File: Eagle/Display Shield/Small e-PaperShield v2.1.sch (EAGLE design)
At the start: 111 parts, among them J2 3300060P1-ST-TF-003A, J3 2.54-8p-male-SMD, J4 2.54-8p-male-SMD, J5 2.54-6p-male-SMD, J6 2.54-6p-male-SMD, J7 2.54-2x3p-female-SMD, Q10 MOSFET-P-044021001, Q11 2N7002, Q2 2N7002, Q3 MOSFET-P-044021001, Q5 MOSFET-P-044021001, Q7 MOSFET-P-044021001, Q8 2N7002, Q9 2N7002, U2 XC6206-3.3-1300260P1, U3 74VHC125PW, U4 74VHC125PW, U5 GT20L16P1Y, U9 S-8120CNB-DRB-TF-G//200021001, X1 FH12-40S-0.5SH

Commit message: added pull-ups for buttons on display shield
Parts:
- added R15, R17, R5, R6: 10k, Discrete:R-0603
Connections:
- net BTN0: now also R5.2
- net BTN1: now also R6.2
- net BTN2: now also R15.2
- net BTN3: now also R17.2
- net LED0: now also J3.1; no longer J3.2
- net LED1: now also J3.2; no longer J3.1
- net M_VCC_3V3: now also R15.1, R17.1, R5.1, R6.1
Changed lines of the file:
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@@
 <part name="SUPPLY3" library="supply2" deviceset="GND" device=""/>
 <part name="SUPPLY4" library="supply2" deviceset="GND" device=""/>
+<part name="R5" library="Discrete" deviceset="R*" device="-0603" value="10k"/>
+<part name="R6" library="Discrete" deviceset="R*" device="-0603" value="10k"/>
+<part name="R15" library="Discrete" deviceset="R*" device="-0603" value="10k"/>
+<part name="R17" library="Discrete" deviceset="R*" device="-0603" value="10k"/>
 </parts>
 <sheets>
@@
 <instance part="SUPPLY3" gate="GND" x="284.48" y="116.84"/>
 <instance part="SUPPLY4" gate="GND" x="287.02" y="142.24"/>
+<instance part="R5" gate="R" x="295.91" y="157.48" rot="MR0"/>
+<instance part="R6" gate="R" x="295.91" y="132.08" rot="MR0"/>
+<instance part="R15" gate="R" x="297.18" y="106.68" rot="MR0"/>
+<instance part="R17" gate="R" x="295.91" y="81.28" rot="MR0"/>
 </instances>
 <busses>
@@
 <label x="-245.11" y="127" size="1.27" layer="95" ratio="10" rot="R180"/>
 </segment>
+<segment>
+<pinref part="R5" gate="R" pin="1"/>
+<wire x1="299.72" y1="157.48" x2="309.88" y2="157.48" width="0.1524" layer="91"/>
+<label x="302.26" y="157.48" size="1.778" layer="95"/>
+</segment>
+<segment>
+<pinref part="R6" gate="R" pin="1"/>
+<wire x1="299.72" y1="132.08" x2="308.61" y2="132.08" width="0.1524" layer="91"/>
+<label x="302.26" y="132.08" size="1.778" layer="95"/>
+</segment>
+<segment>
+<pinref part="R15" gate="R" pin="1"/>
+<wire x1="300.99" y1="106.68" x2="307.34" y2="106.68" width="0.1524" layer="91"/>
+<wire x1="307.34" y1="106.68" x2="308.61" y2="106.68" width="0.1524" layer="91"/>
+<label x="302.26" y="106.68" size="1.778" layer="95"/>
+</segment>
+<segment>
+<pinref part="R17" gate="R" pin="1"/>
+<wire x1="299.72" y1="81.28" x2="308.61" y2="81.28" width="0.1524" layer="91"/>
+<label x="302.26" y="81.28" size="1.778" layer="95"/>
+</segment>
 </net>
 <net name="M_VCC_5V" class="0">
@@
 </segment>
 <segment>
+<pinref part="J3" gate="J" pin="2"/>
+<wire x1="471.17" y1="137.16" x2="471.17" y2="143.51" width="0.1524" layer="91"/>
+<label x="471.17" y="138.43" size="1.778" layer="95" rot="R90"/>
+</segment>
+</net>
+<net name="LED0" class="0">
+<segment>
+<wire x1="300.99" y1="53.34" x2="300.99" y2="57.15" width="0.1524" layer="91"/>
+<label x="300.99" y="57.15" size="1.778" layer="95" rot="R90" xref="yes"/>
+<pinref part="R1" gate="G$1" pin="2"/>
+</segment>
+<segment>
 <pinref part="J3" gate="J" pin="1"/>
 <wire x1="473.71" y1="137.16" x2="473.71" y2="143.51" width="0.1524" layer="91"/>
 <label x="473.71" y="138.43" size="1.778" layer="95" rot="R90"/>
-</segment>
-</net>
-<net name="LED0" class="0">
-<segment>
-<wire x1="300.99" y1="53.34" x2="300.99" y2="57.15" width="0.1524" layer="91"/>
-<label x="300.99" y="57.15" size="1.778" layer="95" rot="R90" xref="yes"/>
-<pinref part="R1" gate="G$1" pin="2"/>
-</segment>
-<segment>
-<pinref part="J3" gate="J" pin="2"/>
-<wire x1="471.17" y1="137.16" x2="471.17" y2="143.51" width="0.1524" layer="91"/>
-<label x="471.17" y="138.43" size="1.778" layer="95" rot="R90"/>
 </segment>
 </net>
@@
 <junction x="281.94" y="81.28"/>
 <wire x1="281.94" y1="81.28" x2="287.02" y2="81.28" width="0.1524" layer="91"/>
+<pinref part="R17" gate="R" pin="2"/>
+<wire x1="287.02" y1="81.28" x2="292.1" y2="81.28" width="0.1524" layer="91"/>
 </segment>
 <segment>
@@
 <junction x="281.94" y="106.68"/>
 <wire x1="281.94" y1="106.68" x2="287.02" y2="106.68" width="0.1524" layer="91"/>
+<pinref part="R15" gate="R" pin="2"/>
+<wire x1="287.02" y1="106.68" x2="293.37" y2="106.68" width="0.1524" layer="91"/>
 </segment>
 <segment>
@@
 <pinref part="S7" gate="G$1" pin="4"/>
 <junction x="281.94" y="132.08"/>
+<pinref part="R6" gate="R" pin="2"/>
+<wire x1="292.1" y1="132.08" x2="287.02" y2="132.08" width="0.1524" layer="91"/>
 </segment>
 <segment>
@@
 <pinref part="S8" gate="G$1" pin="4"/>
 <junction x="281.94" y="157.48"/>
-</segment>
-<segment>
+<pinref part="R5" gate="R" pin="2"/>
+<wire x1="287.02" y1="157.48" x2="292.1" y2="157.48" width="0.1524" layer="91"/>
+</segment>
+<segment>

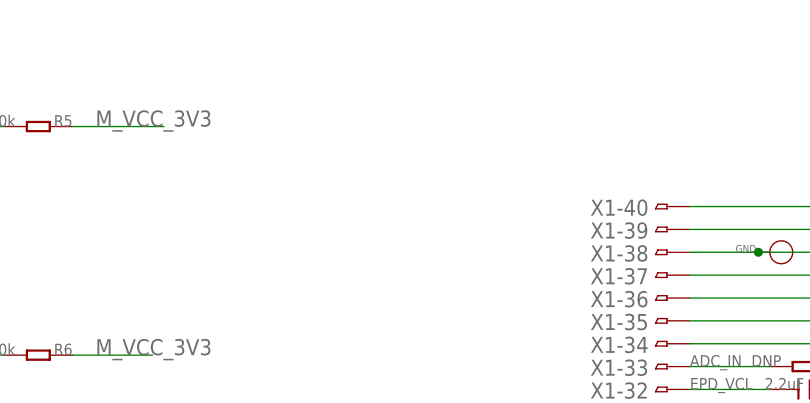
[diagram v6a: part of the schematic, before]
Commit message: resized display shield, placed buttons and leds to their final position
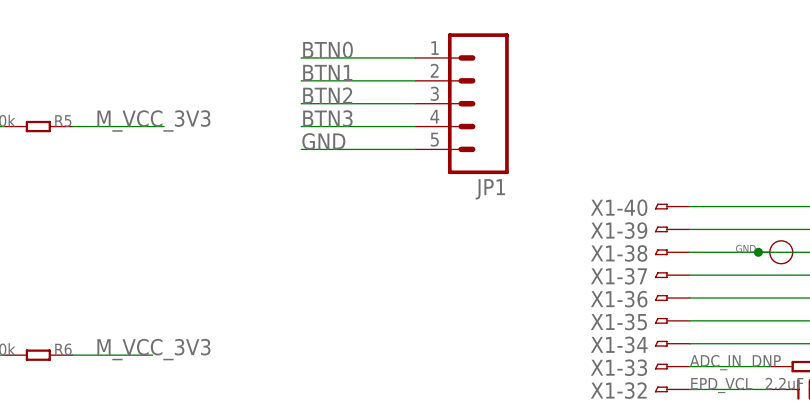
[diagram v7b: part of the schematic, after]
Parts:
- added JP1: (no value), SparkFun-Connectors:M05PTH_LONGPADS
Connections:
- net BTN0: now also JP1.1
- net BTN1: now also JP1.2
- net BTN2: now also JP1.3
- net BTN3: now also JP1.4
- net GND: now also JP1.5
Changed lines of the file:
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@@
 <setting verticaltext="up"/>
 </settings>
-<grid distance="0.05" unitdist="inch" unit="inch" style="lines" multiple="1" display="no" altdistance="0.01" altunitdist="inch" altunit="inch"/>
+<grid distance="0.1" unitdist="inch" unit="inch" style="lines" multiple="1" display="no" altdistance="0.01" altunitdist="inch" altunit="inch"/>
 <layers>
 <layer number="1" name="Top" color="4" fill="1" visible="no" active="no"/>
@@
 <layer number="111" name="111" color="7" fill="1" visible="no" active="no"/>
 <layer number="112" name="tSilk" color="7" fill="1" visible="no" active="no"/>
+<layer number="113" name="IDFDebug" color="4" fill="1" visible="no" active="yes"/>
 <layer number="116" name="Patch_BOT" color="7" fill="1" visible="no" active="no"/>
 <layer number="118" name="Rect_Pads" color="7" fill="1" visible="no" active="no"/>
@@
 <part name="R15" library="Discrete" deviceset="R*" device="-0603" value="10k"/>
 <part name="R17" library="Discrete" deviceset="R*" device="-0603" value="10k"/>
+<part name="JP1" library="SparkFun-Connectors" deviceset="M05" device="PTH_LONGPADS"/>
 </parts>
 <sheets>
@@
 <instance part="R15" gate="R" x="297.18" y="106.68" rot="MR0"/>
 <instance part="R17" gate="R" x="295.91" y="81.28" rot="MR0"/>
+<instance part="JP1" gate="G$1" x="345.44" y="160.02" rot="R180"/>
 </instances>
 <busses>
@@
 <wire x1="300.99" y1="33.02" x2="300.99" y2="31.75" width="0.1524" layer="91"/>
 </segment>
+<segment>
+<pinref part="JP1" gate="G$1" pin="5"/>
+<wire x1="337.82" y1="154.94" x2="325.12" y2="154.94" width="0.1524" layer="91"/>
+<label x="325.12" y="154.94" size="1.778" layer="95"/>
+</segment>
 </net>
 <net name="M_MOSI" class="0">
@@
 <label x="471.17" y="68.58" size="1.778" layer="95" rot="R90"/>
 </segment>
+<segment>
+<pinref part="JP1" gate="G$1" pin="4"/>
+<wire x1="337.82" y1="157.48" x2="325.12" y2="157.48" width="0.1524" layer="91"/>
+<label x="325.12" y="157.48" size="1.778" layer="95"/>
+</segment>
 </net>
 <net name="BTN2" class="0">
@@
 <wire x1="468.63" y1="76.2" x2="468.63" y2="68.58" width="0.1524" layer="91"/>
 <label x="468.63" y="68.58" size="1.778" layer="95" rot="R90"/>
+</segment>
+<segment>
+<pinref part="JP1" gate="G$1" pin="3"/>
+<wire x1="337.82" y1="160.02" x2="325.12" y2="160.02" width="0.1524" layer="91"/>
+<label x="325.12" y="160.02" size="1.778" layer="95"/>
 </segment>
 </net>
@@
 <label x="466.09" y="68.58" size="1.778" layer="95" rot="R90"/>
 </segment>
+<segment>
+<pinref part="JP1" gate="G$1" pin="2"/>
+<wire x1="337.82" y1="162.56" x2="325.12" y2="162.56" width="0.1524" layer="91"/>
+<label x="325.12" y="162.56" size="1.778" layer="95"/>
+</segment>
 </net>
 <net name="BTN0" class="0">
@@
 <label x="463.55" y="68.58" size="1.778" layer="95" rot="R90"/>
 </segment>
-</net>
+<segment>
+<pinref part="JP1" gate="G$1" pin="1"/>
+<wire x1="337.82" y1="165.1" x2="325.12" y2="165.1" width="0.1524" layer="91"/>
+<label x="325.12" y="165.1" size="1.778" layer="95"/>
+</segment>
+</net>
